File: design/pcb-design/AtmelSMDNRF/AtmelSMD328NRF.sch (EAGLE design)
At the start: 13 parts, among them J1 MICRO-USB-ZX62R-B-5P, U1 ATMEGA328P

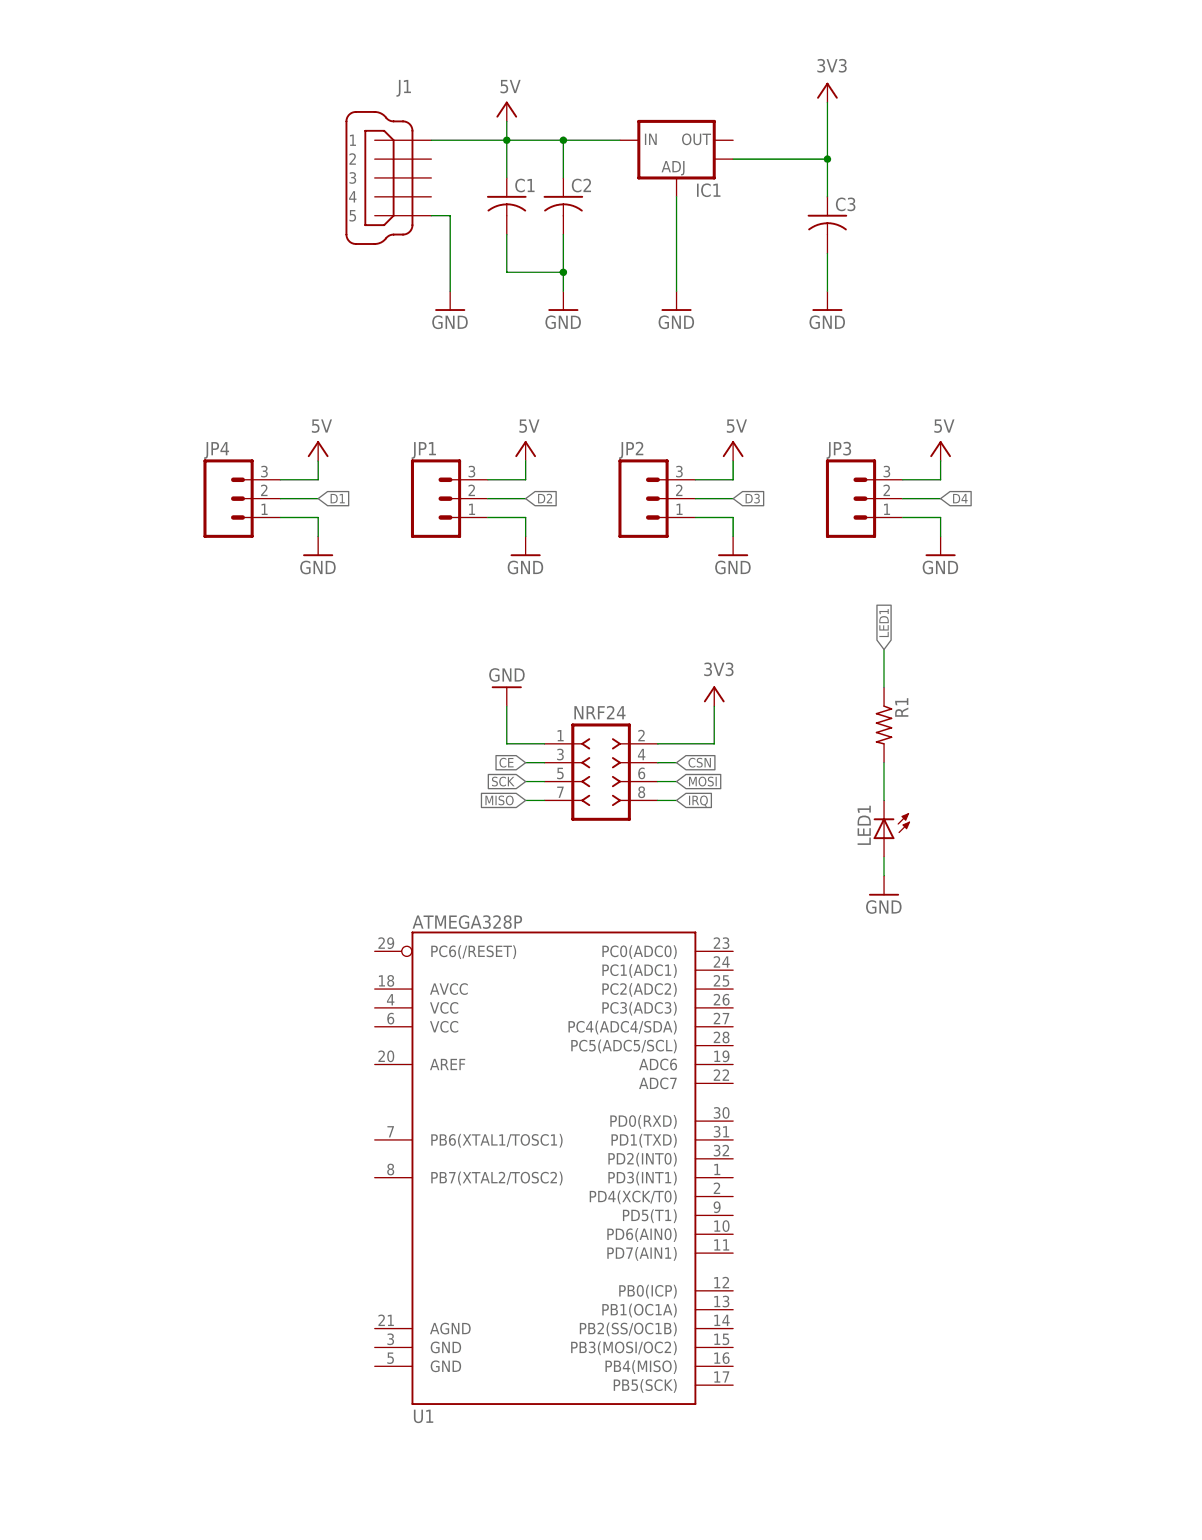
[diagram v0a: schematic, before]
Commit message: pcb design: sensor hub update
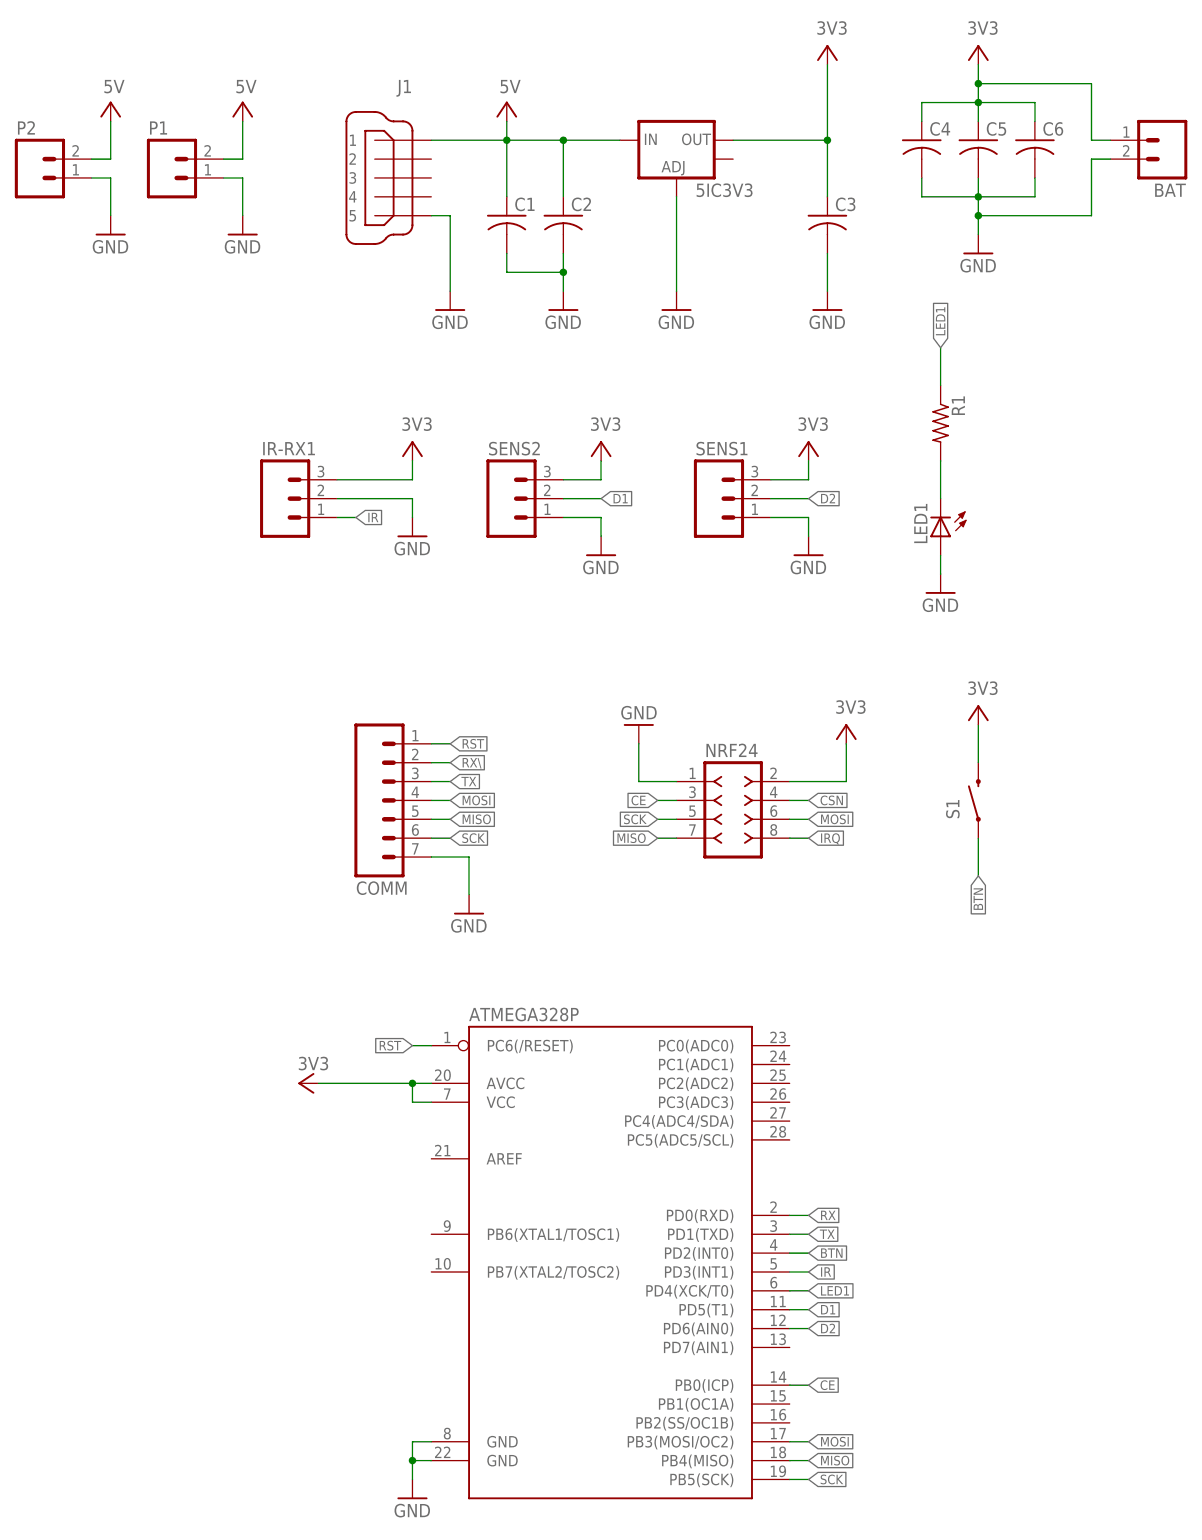
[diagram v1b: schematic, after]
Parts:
- removed JP1, JP2, JP3, JP4: (no value), sparkFun-Connectors:M03PTH
- removed U1: ATMEGA328P, sparkFun-DigitalIC:ATMEGA328_SMT
- added ATMEGA328P: ATMEGA328P_PDIP, sparkFun-DigitalIC:ATMEGA328P_PDIP
- added BAT, P1, P2: M02PTH, sparkFun-Connectors:M02PTH
- added C4, C5, C6: (no value), resistor:C-USC0805
- added COMM: (no value), sparkFun-Connectors:M07
- added IR-RX1, SENS1, SENS2: (no value), sparkFun-Connectors:M03PTH
- added S1: SWITCH-MOMENTARY-2SMD-1101NE, sparkFun-Electromechanical:SWITCH-MOMENTARY-2SMD-1101NE
- renumbered IC1 to 5IC3V3
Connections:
- removed net D3: JP2.2
- removed net D4: JP3.2
- new net BTN: ATMEGA328P.PD2(INT0), S1.1
- new net IR: ATMEGA328P.PD3(INT1), IR-RX1.1
- new net RST: ATMEGA328P.PC6(/RESET), COMM.1
- new net RX: ATMEGA328P.PD0(RXD)
- new net RX\: COMM.2
- new net TX: ATMEGA328P.PD1(TXD), COMM.3
- net +3V3: now also 5IC3V3.OUT, ATMEGA328P.AVCC, ATMEGA328P.VCC, BAT.1, C4.1, C5.1, C6.1, IR-RX1.3, S1.2, SENS1.3, SENS2.3; no longer 5IC3V3.OUT@1
- net +5V: now also P1.2, P2.2; no longer JP1.3, JP2.3, JP3.3, JP4.3
- net CE: now also ATMEGA328P.PB0(ICP)
- net D1: now also ATMEGA328P.PD5(T1), SENS2.2; no longer JP4.2
- net D2: now also ATMEGA328P.PD6(AIN0), SENS1.2; no longer JP1.2
- net GND: now also ATMEGA328P.GND@1, ATMEGA328P.GND@2, BAT.2, C4.2, C5.2, C6.2, COMM.7, IR-RX1.2, P1.1, P2.1, SENS1.1, SENS2.1; no longer JP1.1, JP2.1, JP3.1, JP4.1
- net LED1: now also ATMEGA328P.PD4(XCK/T0)
- net MISO: now also ATMEGA328P.PB4(MISO), COMM.5
- net MOSI: now also ATMEGA328P.PB3(MOSI/OC2), COMM.4
- net SCK: now also ATMEGA328P.PB5(SCK), COMM.6
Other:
- moved on the sheet: C1, C2, LED1, NRF24, R1
